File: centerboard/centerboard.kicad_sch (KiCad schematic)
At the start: 3 parts, among them J1 Conn_02x05_Odd_Even, SW1 SW_Push, U1 ATmega32U4-A

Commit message: centerboard messing around
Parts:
- added J2: USB_B_Micro, Connector_USB:USB_Micro-B_Molex-105017-0001, symbol Connector:USB_B_Micro
- J1: footprint (none) -> Connector_IDC:IDC-Header_2x05_P2.54mm_Vertical
- SW1: footprint (none) -> Button_Switch_SMD:SW_Push_SPST_NO_Alps_SKRK
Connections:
- net GND: now also J2.5 (GND)
- net VCC: now also J2.1 (VBUS)
- net at U1.3 (D-): now also J2.2 (D-)
- net at U1.4 (D+): now also J2.3 (D+)
- net COL_LA: no longer names the net of U1.12 (PB7)
- net COL_LB: no longer names the net of U1.31 (PC6)
- net COL_LC: no longer names the net of U1.32 (PC7)
- net COL_LD: no longer names the net of U1.18 (PD0)
- net COL_LE: no longer names the net of U1.19 (PD1)
- net COL_LF: no longer names the net of U1.20 (PD2)
- net COL_LT: no longer names the net of U1.21 (PD3)
- net COL_RA: no longer names the net of U1.41 (PF0)
- net COL_RB: no longer names the net of U1.40 (PF1)
- net COL_RC: no longer names the net of U1.39 (PF4)
- net COL_RD: no longer names the net of U1.38 (PF5)
- net COL_RE: no longer names the net of U1.28 (PB4)
- net COL_RF: no longer names the net of U1.29 (PB5)
- net COL_RT: no longer names the net of U1.30 (PB6)
- net ROW_1: no longer names the net of U1.25 (PD4)
- net ROW_2: no longer names the net of U1.22 (PD5)
- net ROW_3: no longer names the net of U1.26 (PD6)
- net ROW_4: no longer names the net of U1.27 (PD7)
- no-connect marks 1 -> 3
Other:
- sheet Column renamed Column L1
- removed sheet Column1
- removed sheet Column10
- removed sheet Column11
- removed sheet Column12
- removed sheet Column13
- removed sheet Column2
- removed sheet Column3
- removed sheet Column4
- removed sheet Column5
- removed sheet Column6
- removed sheet Column7
- removed sheet Column8
- removed sheet Column9
- added sheet Column L2 (column.kicad_sch)
- added sheet Column L3 (column.kicad_sch)
- added sheet Column L4 (column.kicad_sch)
- added sheet Column L5 (column.kicad_sch)
- added sheet Column L6 (column.kicad_sch)
- added sheet Column L7 (column.kicad_sch)

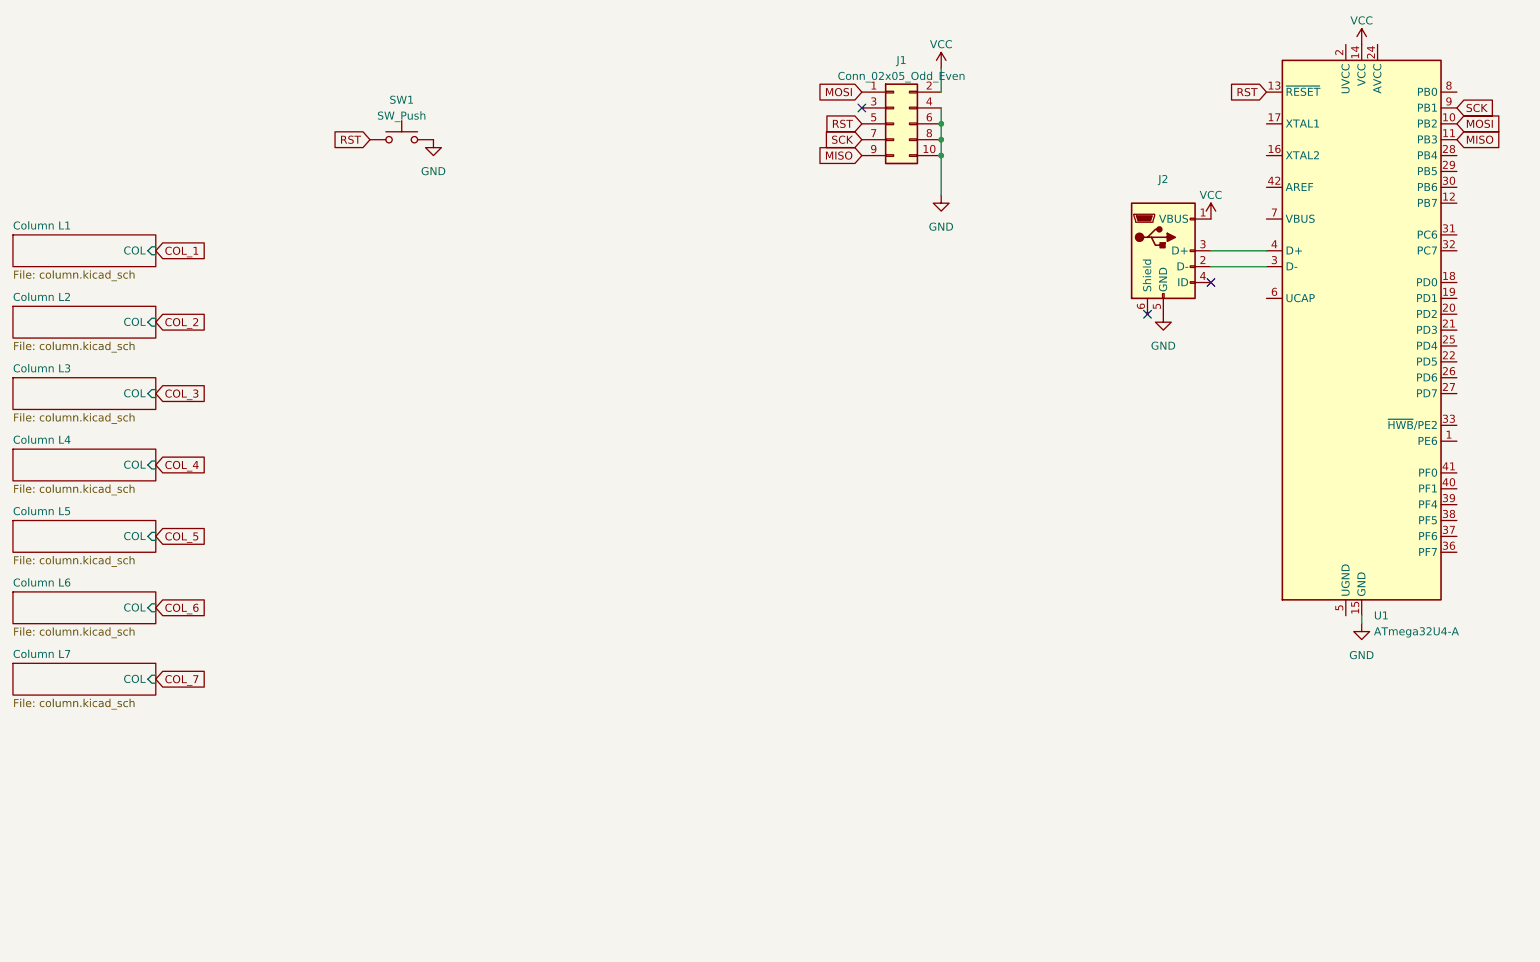
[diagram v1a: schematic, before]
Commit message: Various tweaks. About to flip centerboard, not feeling too confident in the results there
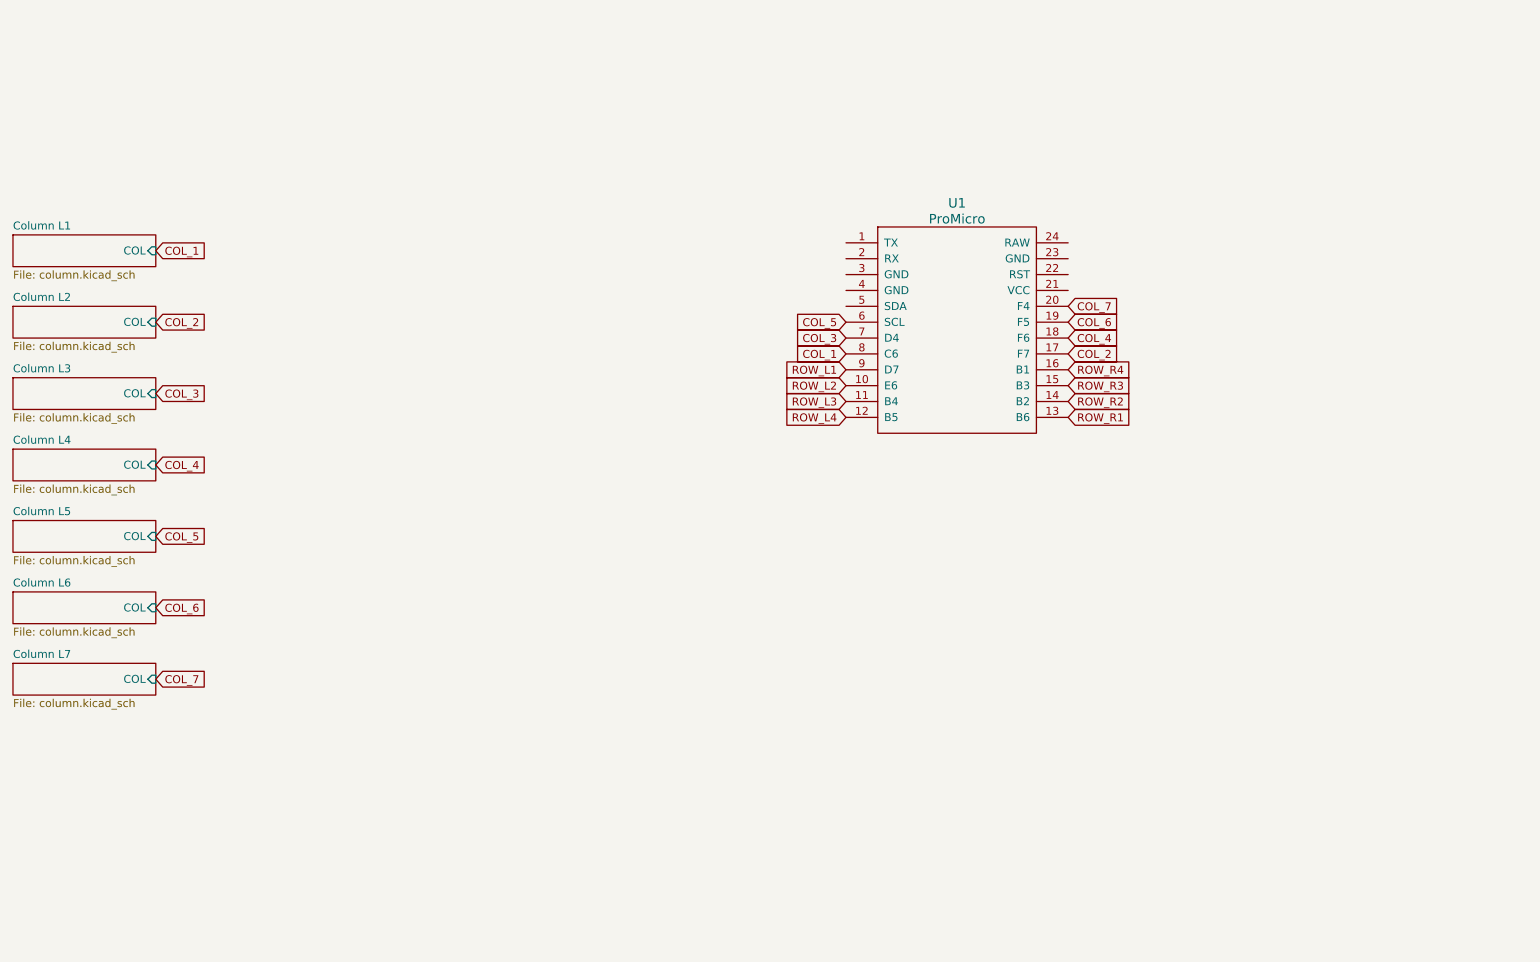
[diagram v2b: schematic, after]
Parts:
- removed J1: Conn_02x05_Odd_Even, Connector_IDC:IDC-Header_2x05_P2.54mm_Vertical, symbol Connector_Generic:Conn_02x05_Odd_Even
- removed J2: USB_B_Micro, Connector_USB:USB_Micro-B_Molex-105017-0001, symbol Connector:USB_B_Micro
- removed SW1: SW_Push, Button_Switch_SMD:SW_Push_SPST_NO_Alps_SKRK, symbol Switch:SW_Push
- removed U1: ATmega32U4-A, Package_QFP:TQFP-44_10x10mm_P0.8mm, symbol MCU_Microchip_ATmega:ATmega32U4-A
- added U1: ProMicro, promicro:ProMicro, symbol promicro:ProMicro
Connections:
- net COL_1: now also U1.8 (C6)
- net COL_2: now also U1.17 (F7)
- net COL_3: now also U1.7 (D4)
- net COL_4: now also U1.18 (F6)
- net COL_5: now also U1.6 (SCL)
- net COL_6: now also U1.19 (F5)
- net COL_7: now also U1.20 (F4)
- new net ROW_L1: U1.9 (D7)
- new net ROW_L2: U1.10 (E6)
- new net ROW_L3: U1.11 (B4)
- new net ROW_L4: U1.12 (B5)
- new net ROW_R1: U1.13 (B6)
- new net ROW_R2: U1.14 (B2)
- new net ROW_R3: U1.15 (B3)
- new net ROW_R4: U1.16 (B1)
- no-connect marks 3 -> 0

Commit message: misc tidying
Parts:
- added SW1: SW_Push, Button_Switch_THT:SW_PUSH_6mm, symbol Switch:SW_Push
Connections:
- net at U1.22 (RST): now also SW1.2
- net at U1.23 (GND): now also SW1.1
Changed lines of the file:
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@@
 (kicad_sch (version 20230121) (generator eeschema)
   (paper "A4")
+  (wire (pts (xy 222.25 54.61) (xy 205.74 54.61))
+    (stroke (width 0) (type default))
+  )
+  (wire (pts (xy 222.25 52.07) (xy 222.25 54.61))
+    (stroke (width 0) (type default))
+  )
+  (wire (pts (xy 205.74 52.07) (xy 212.09 52.07))
+    (stroke (width 0) (type default))
+  )
   (global_label "COL_7" (shape input) (at 205.74 59.69 0) (fields_autoplaced)
     (effects (font (size 1.27 1.27)) (justify left))
@@
         )
       )
+    )
+  )
+  (symbol (lib_id "Switch:SW_Push") (at 217.17 52.07 0) (unit 1)
+    (in_bom yes) (on_board yes) (dnp no) (fields_autoplaced)
+    (property "Reference" "SW1" (at 217.17 45.72 0)
+      (effects (font (size 1.27 1.27)))
+    )
+    (property "Value" "SW_Push" (at 217.17 48.26 0)
+      (effects (font (size 1.27 1.27)))
+    )
+    (property "Footprint" "Button_Switch_THT:SW_PUSH_6mm" (at 217.17 46.99 0)
+      (effects (font (size 1.27 1.27)) hide)
+    )
+    (property "Datasheet" "~" (at 217.17 46.99 0)
+      (effects (font (size 1.27 1.27)) hide)
+    )
+    (pin "1")
+    (pin "2")
+    (instances
+      (project "centerboard"
+        (path "/4cf5c873-f5e9-4261-911c-886f387fb0f3"
+          (reference "SW1") (unit 1)
+        )
+      )

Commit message: centerboard redone, in 1.0 form I think
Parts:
- removed SW1: SW_Push, Button_Switch_THT:SW_PUSH_6mm, symbol Switch:SW_Push
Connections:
- net COL_1: now also U1.6 (SCL); no longer U1.8 (C6)
- net COL_2: now also U1.13 (B6); no longer U1.17 (F7)
- net COL_3: now also U1.19 (F5); no longer U1.7 (D4)
- net COL_4: now also U1.12 (B5); no longer U1.18 (F6)
- net COL_5: now also U1.5 (SDA); no longer U1.6 (SCL)
- net COL_6: now also U1.14 (B2); no longer U1.19 (F5)
- net ROW_L1: now also U1.7 (D4); no longer U1.9 (D7)
- net ROW_L2: now also U1.8 (C6); no longer U1.10 (E6)
- net ROW_L3: now also U1.9 (D7); no longer U1.11 (B4)
- net ROW_L4: now also U1.10 (E6); no longer U1.12 (B5)
- net ROW_R1: now also U1.18 (F6); no longer U1.13 (B6)
- net ROW_R2: now also U1.17 (F7); no longer U1.14 (B2)
- net ROW_R3: now also U1.16 (B1); no longer U1.15 (B3)
- net ROW_R4: now also U1.15 (B3); no longer U1.16 (B1)
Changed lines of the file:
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@@
 (kicad_sch (version 20230121) (generator eeschema)
   (paper "A4")
-  (wire (pts (xy 222.25 54.61) (xy 205.74 54.61))
-    (stroke (width 0) (type default))
-  )
-  (wire (pts (xy 222.25 52.07) (xy 222.25 54.61))
-    (stroke (width 0) (type default))
-  )
-  (wire (pts (xy 205.74 52.07) (xy 212.09 52.07))
-    (stroke (width 0) (type default))
-  )
   (global_label "COL_7" (shape input) (at 205.74 59.69 0) (fields_autoplaced)
     (effects (font (size 1.27 1.27)) (justify left))
@@
     )
   )
-  (global_label "ROW_R1" (shape input) (at 205.74 77.47 0) (fields_autoplaced)
+  (global_label "ROW_R1" (shape input) (at 205.74 64.77 0) (fields_autoplaced)
     (effects (font (size 1.27 1.27)) (justify left))
-    (property "Intersheetrefs" "${INTERSHEET_REFS}" (at 216.1448 77.47 0)
+    (property "Intersheetrefs" "${INTERSHEET_REFS}" (at 216.1448 64.77 0)
       (effects (font (size 1.27 1.27)) (justify left) hide)
     )
   )
-  (global_label "ROW_R2" (shape input) (at 205.74 74.93 0) (fields_autoplaced)
+  (global_label "ROW_R2" (shape input) (at 205.74 67.31 0) (fields_autoplaced)
     (effects (font (size 1.27 1.27)) (justify left))
-    (property "Intersheetrefs" "${INTERSHEET_REFS}" (at 216.1448 74.93 0)
+    (property "Intersheetrefs" "${INTERSHEET_REFS}" (at 216.1448 67.31 0)
       (effects (font (size 1.27 1.27)) (justify left) hide)
     )
@@
     )
   )
-  (global_label "COL_6" (shape input) (at 205.74 62.23 0) (fields_autoplaced)
+  (global_label "COL_6" (shape input) (at 205.74 74.93 0) (fields_autoplaced)
     (effects (font (size 1.27 1.27)) (justify left))
-    (property "Intersheetrefs" "${INTERSHEET_REFS}" (at 214.4515 62.23 0)
+    (property "Intersheetrefs" "${INTERSHEET_REFS}" (at 214.4515 74.93 0)
       (effects (font (size 1.27 1.27)) (justify left) hide)
     )
@@
     )
   )
-  (global_label "COL_1" (shape input) (at 170.18 67.31 180) (fields_autoplaced)
-    (effects (font (size 1.27 1.27)) (justify right))
-    (property "Intersheetrefs" "${INTERSHEET_REFS}" (at 161.4685 67.31 0)
-      (effects (font (size 1.27 1.27)) (justify right) hide)
-    )
-  )
-  (global_label "COL_5" (shape input) (at 170.18 62.23 180) (fields_autoplaced)
+  (global_label "COL_1" (shape input) (at 170.18 62.23 180) (fields_autoplaced)
     (effects (font (size 1.27 1.27)) (justify right))
     (property "Intersheetrefs" "${INTERSHEET_REFS}" (at 161.4685 62.23 0)
@@
     )
   )
-  (global_label "COL_2" (shape input) (at 205.74 67.31 0) (fields_autoplaced)
+  (global_label "COL_5" (shape input) (at 170.18 59.69 180) (fields_autoplaced)
+    (effects (font (size 1.27 1.27)) (justify right))
+    (property "Intersheetrefs" "${INTERSHEET_REFS}" (at 161.4685 59.69 0)
+      (effects (font (size 1.27 1.27)) (justify right) hide)
+    )
+  )
+  (global_label "COL_2" (shape input) (at 205.74 77.47 0) (fields_autoplaced)
     (effects (font (size 1.27 1.27)) (justify left))
-    (property "Intersheetrefs" "${INTERSHEET_REFS}" (at 214.4515 67.31 0)
+    (property "Intersheetrefs" "${INTERSHEET_REFS}" (at 214.4515 77.47 0)
       (effects (font (size 1.27 1.27)) (justify left) hide)
     )
   )
-  (global_label "COL_3" (shape input) (at 170.18 64.77 180) (fields_autoplaced)
-    (effects (font (size 1.27 1.27)) (justify right))
-    (property "Intersheetrefs" "${INTERSHEET_REFS}" (at 161.4685 64.77 0)
-      (effects (font (size 1.27 1.27)) (justify right) hide)
+  (global_label "COL_3" (shape input) (at 205.74 62.23 0) (fields_autoplaced)
+    (effects (font (size 1.27 1.27)) (justify left))
+    (property "Intersheetrefs" "${INTERSHEET_REFS}" (at 214.4515 62.23 0)
+      (effects (font (size 1.27 1.27)) (justify left) hide)
     )
   )
@@
     )
   )
-  (global_label "ROW_R4" (shape input) (at 205.74 69.85 0) (fields_autoplaced)
+  (global_label "ROW_R4" (shape input) (at 205.74 72.39 0) (fields_autoplaced)
     (effects (font (size 1.27 1.27)) (justify left))
-    (property "Intersheetrefs" "${INTERSHEET_REFS}" (at 216.1448 69.85 0)
+    (property "Intersheetrefs" "${INTERSHEET_REFS}" (at 216.1448 72.39 0)
       (effects (font (size 1.27 1.27)) (justify left) hide)
     )
   )
-  (global_label "ROW_L4" (shape input) (at 170.18 77.47 180) (fields_autoplaced)
+  (global_label "ROW_L4" (shape input) (at 170.18 72.39 180) (fields_autoplaced)
     (effects (font (size 1.27 1.27)) (justify right))
-    (property "Intersheetrefs" "${INTERSHEET_REFS}" (at 160.0171 77.47 0)
+    (property "Intersheetrefs" "${INTERSHEET_REFS}" (at 160.0171 72.39 0)
       (effects (font (size 1.27 1.27)) (justify right) hide)
     )
@@
     )
   )
-  (global_label "COL_4" (shape input) (at 205.74 64.77 0) (fields_autoplaced)
-    (effects (font (size 1.27 1.27)) (justify left))
-    (property "Intersheetrefs" "${INTERSHEET_REFS}" (at 214.4515 64.77 0)
-      (effects (font (size 1.27 1.27)) (justify left) hide)
+  (global_label "COL_4" (shape input) (at 170.18 77.47 180) (fields_autoplaced)
+    (effects (font (size 1.27 1.27)) (justify right))
+    (property "Intersheetrefs" "${INTERSHEET_REFS}" (at 161.4685 77.47 0)
+      (effects (font (size 1.27 1.27)) (justify right) hide)
     )
   )
-  (global_label "ROW_L2" (shape input) (at 170.18 72.39 180) (fields_autoplaced)
+  (global_label "ROW_L2" (shape input) (at 170.18 67.31 180) (fields_autoplaced)
     (effects (font (size 1.27 1.27)) (justify right))
-    (property "Intersheetrefs" "${INTERSHEET_REFS}" (at 160.0171 72.39 0)
+    (property "Intersheetrefs" "${INTERSHEET_REFS}" (at 160.0171 67.31 0)
       (effects (font (size 1.27 1.27)) (justify right) hide)
     )
@@
     )
   )
-  (global_label "ROW_L1" (shape input) (at 170.18 69.85 180) (fields_autoplaced)
+  (global_label "ROW_L1" (shape input) (at 170.18 64.77 180) (fields_autoplaced)
     (effects (font (size 1.27 1.27)) (justify right))
-    (property "Intersheetrefs" "${INTERSHEET_REFS}" (at 160.0171 69.85 0)
+    (property "Intersheetrefs" "${INTERSHEET_REFS}" (at 160.0171 64.77 0)
       (effects (font (size 1.27 1.27)) (justify right) hide)
     )
   )
-  (global_label "ROW_R3" (shape input) (at 205.74 72.39 0) (fields_autoplaced)
+  (global_label "ROW_R3" (shape input) (at 205.74 69.85 0) (fields_autoplaced)
     (effects (font (size 1.27 1.27)) (justify left))
-    (property "Intersheetrefs" "${INTERSHEET_REFS}" (at 216.1448 72.39 0)
+    (property "Intersheetrefs" "${INTERSHEET_REFS}" (at 216.1448 69.85 0)
       (effects (font (size 1.27 1.27)) (justify left) hide)
     )
@@
     )
   )
-  (global_label "ROW_L3" (shape input) (at 170.18 74.93 180) (fields_autoplaced)
+  (global_label "ROW_L3" (shape input) (at 170.18 69.85 180) (fields_autoplaced)
     (effects (font (size 1.27 1.27)) (justify right))
-    (property "Intersheetrefs" "${INTERSHEET_REFS}" (at 160.0171 74.93 0)
+    (property "Intersheetrefs" "${INTERSHEET_REFS}" (at 160.0171 69.85 0)
       (effects (font (size 1.27 1.27)) (justify right) hide)
     )
@@
         )
       )
-    )
-  )
-  (symbol (lib_id "Switch:SW_Push") (at 217.17 52.07 0) (unit 1)
-    (in_bom yes) (on_board yes) (dnp no) (fields_autoplaced)
-    (property "Reference" "SW1" (at 217.17 45.72 0)
-      (effects (font (size 1.27 1.27)))
-    )
-    (property "Value" "SW_Push" (at 217.17 48.26 0)
-      (effects (font (size 1.27 1.27)))
-    )
-    (property "Footprint" "Button_Switch_THT:SW_PUSH_6mm" (at 217.17 46.99 0)
-      (effects (font (size 1.27 1.27)) hide)
-    )
-    (property "Datasheet" "~" (at 217.17 46.99 0)
-      (effects (font (size 1.27 1.27)) hide)
-    )
-    (pin "1")
-    (pin "2")
-    (instances
-      (project "centerboard"
-        (path "/4cf5c873-f5e9-4261-911c-886f387fb0f3"
-          (reference "SW1") (unit 1)
-        )
-      )
